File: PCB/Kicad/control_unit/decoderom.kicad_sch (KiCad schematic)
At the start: 56 parts

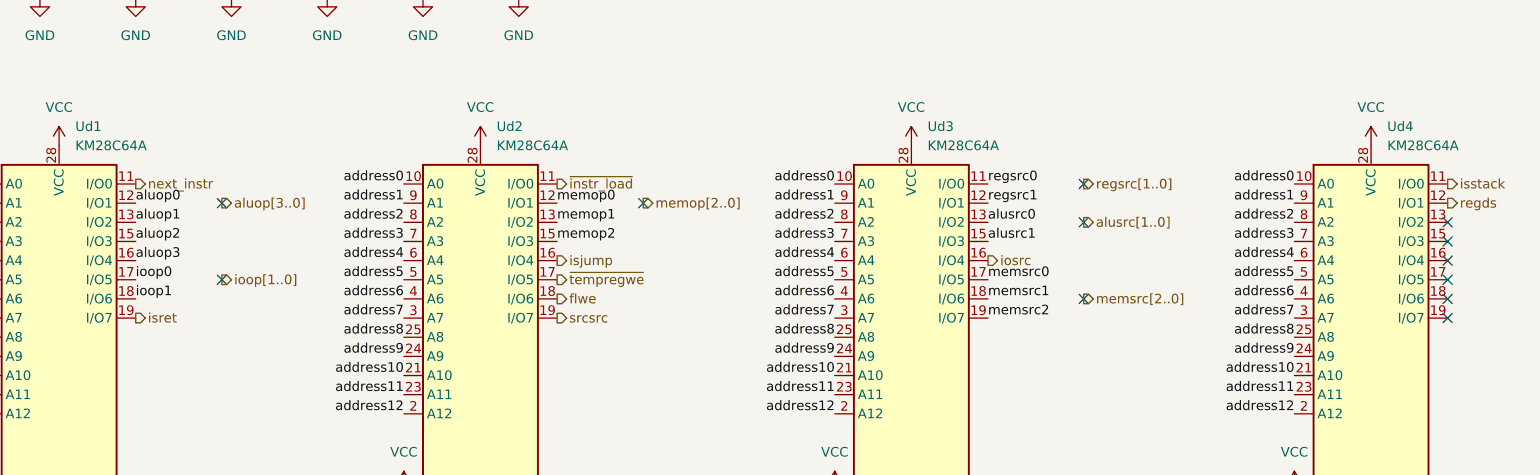
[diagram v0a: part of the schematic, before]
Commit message: control unit logic routing done
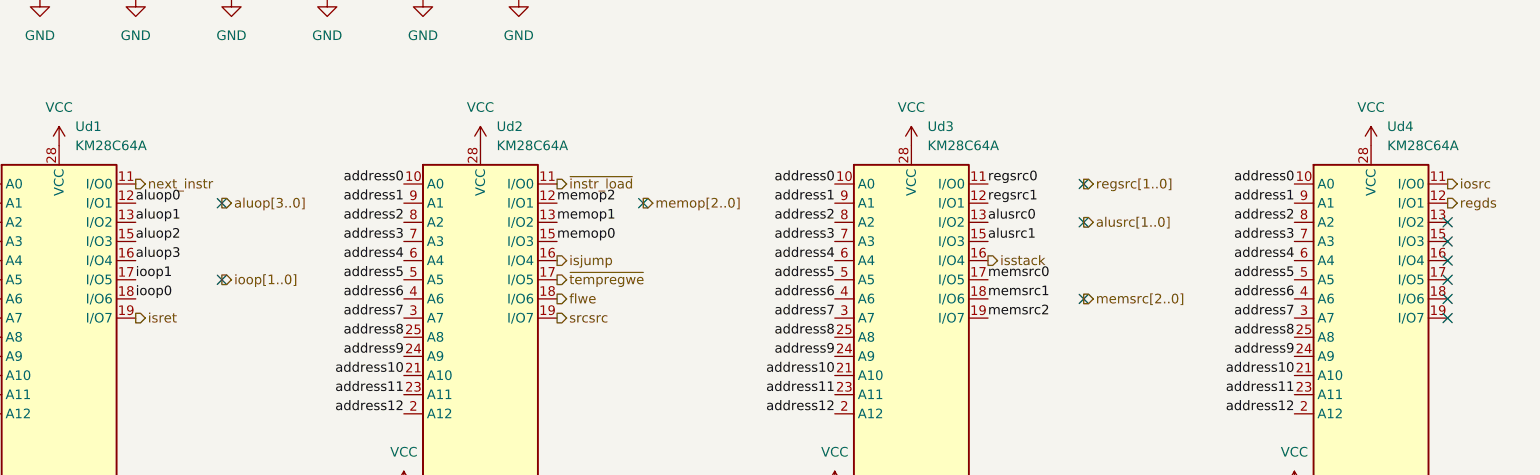
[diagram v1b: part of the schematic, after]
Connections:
- net ioop0: now also Ud1.18 (I/O6); no longer Ud1.17 (I/O5)
- net ioop1: now also Ud1.17 (I/O5); no longer Ud1.18 (I/O6)
- net iosrc: now also Ud4.11 (I/O0); no longer Ud3.16 (I/O4)
- net isstack: now also Ud3.16 (I/O4); no longer Ud4.11 (I/O0)
- net memop0: now also Ud2.15 (I/O3); no longer Ud2.12 (I/O1)
- net memop2: now also Ud2.12 (I/O1); no longer Ud2.15 (I/O3)
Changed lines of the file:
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@@
 	)
 	(label "memop0"
-		(at 138.43 99.695 0)
+		(at 138.43 104.775 0)
 		(effects
 			(font
@@
 	)
 	(label "ioop0"
-		(at 82.55 109.855 0)
+		(at 82.55 112.395 0)
 		(effects
 			(font
@@
 	)
 	(label "ioop1"
-		(at 82.55 112.395 0)
+		(at 82.55 109.855 0)
 		(effects
 			(font
@@
 	)
 	(label "memop2"
-		(at 138.43 104.775 0)
+		(at 138.43 99.695 0)
 		(effects
 			(font
@@
 	(hierarchical_label "iosrc"
 		(shape output)
+		(at 256.54 97.155 0)
+		(effects
+			(font
+				(size 1.27 1.27)
+			)
+			(justify left)
+		)
+	)
+	(hierarchical_label "memop[2..0]"
+		(shape output)
+		(at 149.86 99.695 0)
+		(effects
+			(font
+				(size 1.27 1.27)
+			)
+			(justify left)
+		)
+	)
+	(hierarchical_label "aluop[3..0]"
+		(shape output)
+		(at 93.98 99.695 0)
+		(effects
+			(font
+				(size 1.27 1.27)
+			)
+			(justify left)
+		)
+	)
+	(hierarchical_label "srcsrc"
+		(shape output)
+		(at 138.43 114.935 0)
+		(effects
+			(font
+				(size 1.27 1.27)
+			)
+			(justify left)
+		)
+	)
+	(hierarchical_label "alusrc[1..0]"
+		(shape output)
+		(at 208.28 102.235 0)
+		(effects
+			(font
+				(size 1.27 1.27)
+			)
+			(justify left)
+		)
+	)
+	(hierarchical_label "isstack"
+		(shape output)
 		(at 195.58 107.315 0)
 		(effects
 			(font
-				(size 1.27 1.27)
-			)
-			(justify left)
-		)
-	)
-	(hierarchical_label "memop[2..0]"
-		(shape output)
-		(at 149.86 99.695 0)
-		(effects
-			(font
-				(size 1.27 1.27)
-			)
-			(justify left)
-		)
-	)
-	(hierarchical_label "aluop[3..0]"
-		(shape output)
-		(at 93.98 99.695 0)
-		(effects
-			(font
-				(size 1.27 1.27)
-			)
-			(justify left)
-		)
-	)
-	(hierarchical_label "srcsrc"
-		(shape output)
-		(at 138.43 114.935 0)
-		(effects
-			(font
-				(size 1.27 1.27)
-			)
-			(justify left)
-		)
-	)
-	(hierarchical_label "alusrc[1..0]"
-		(shape output)
-		(at 208.28 102.235 0)
-		(effects
-			(font
-				(size 1.27 1.27)
-			)
-			(justify left)
-		)
-	)
-	(hierarchical_label "isstack"
-		(shape output)
-		(at 256.54 97.155 0)
-		(effects
-			(font
